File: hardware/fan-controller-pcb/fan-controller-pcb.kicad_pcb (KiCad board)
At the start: 2 copper layers, 100 x 130 mm, 53 parts, among them J1 Screw_Terminal_01x04, J2 nc3fdm3-v, J3 nc3mdm3-v, SW1 SW_SPDT, SW2 SW_DIP_x10, U1 MC7812BDTG, U2 MC7805CDTG, U3 MCP4922, U4 TLC272, U5 MAX485E

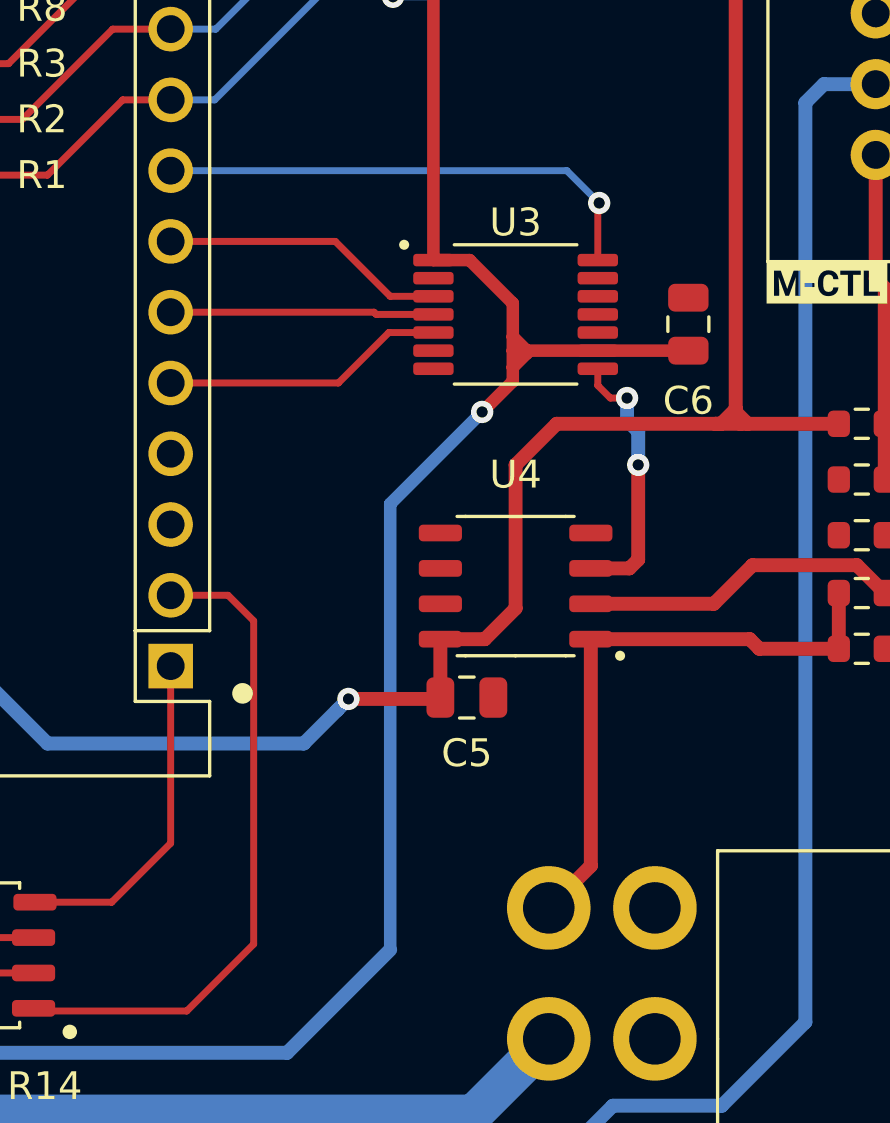
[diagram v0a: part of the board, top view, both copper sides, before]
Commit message: Fix the MCP4922 footprint and adapting the traces
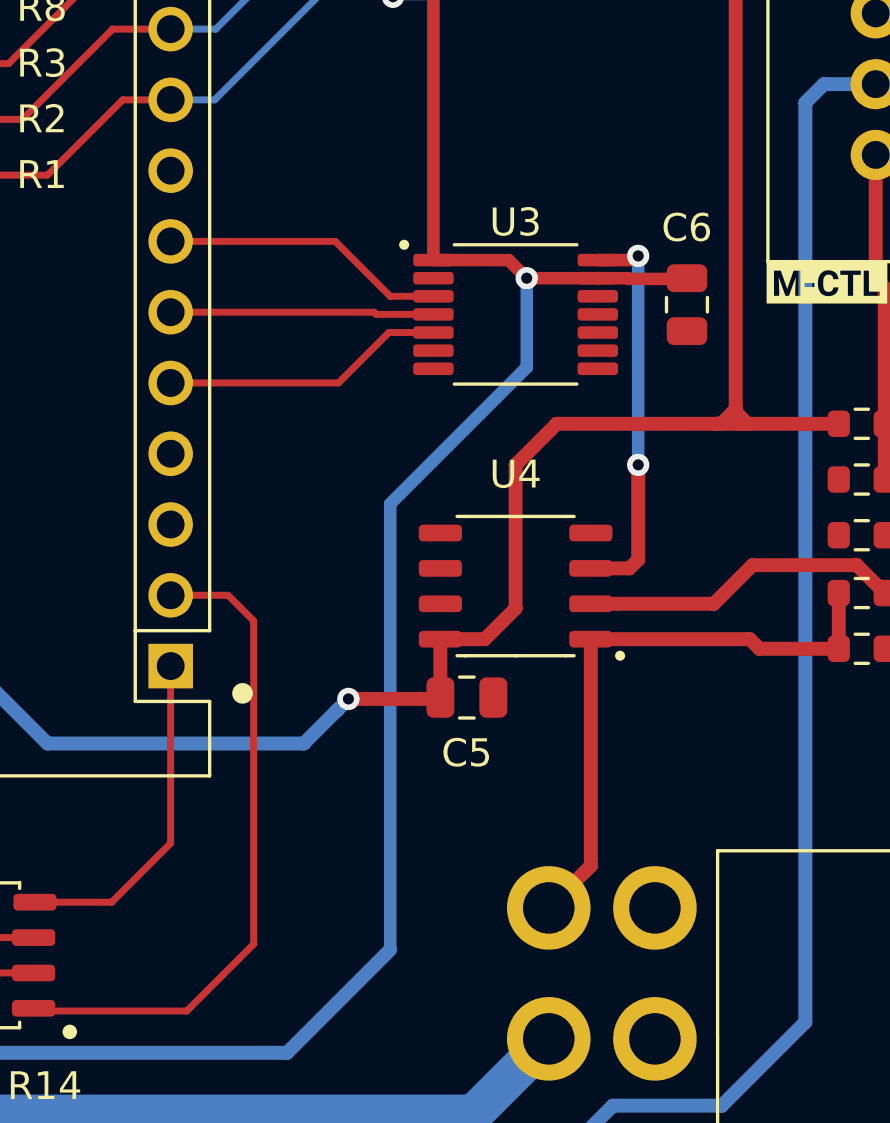
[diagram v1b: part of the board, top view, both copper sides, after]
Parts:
- moved C6 0.70 mm to (146.2, 92.7), turned to -90 degrees
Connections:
- A1 pad 8: Net-(A1-Pad8) -> unconnected-(A1-Pad8)
- R15 pad 1: Net-(R15-Pad1) -> 0-10V_Fan_Control
- R15 pad 2: 0-10V_Fan_Control -> Net-(R17-Pad1)
- R17 pad 1: 0-10V_Fan_Control -> Net-(R17-Pad1)
- U3 pad 8: Net-(A1-Pad8) -> unconnected-(U3-Pad8)
- U4 pad 2: Net-(R15-Pad1) -> Net-(R17-Pad1)
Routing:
- net Net-(A1-Pad8): track 17.9 -> 0.00 mm, vias 1 -> 0
- net Net-(R17-Pad1): track 0.00 -> 11.5 mm
- net Net-(R15-Pad1): track 11.5 -> 0.00 mm
- net Net-(U3-Pad14): track 9.63 -> 14.2 mm
- net +5V: track 140.1 -> 139.3 mm

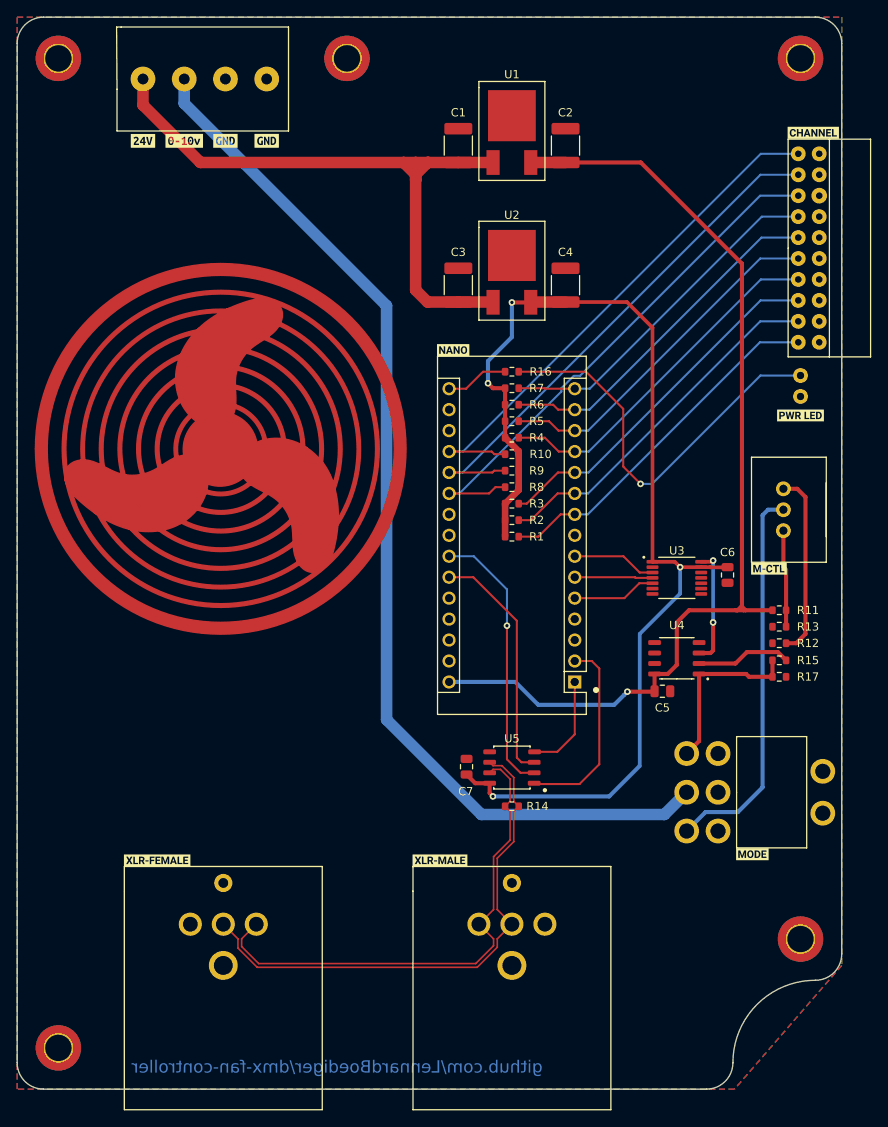
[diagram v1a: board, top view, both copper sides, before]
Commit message: minor routing improvements and adding gerber files
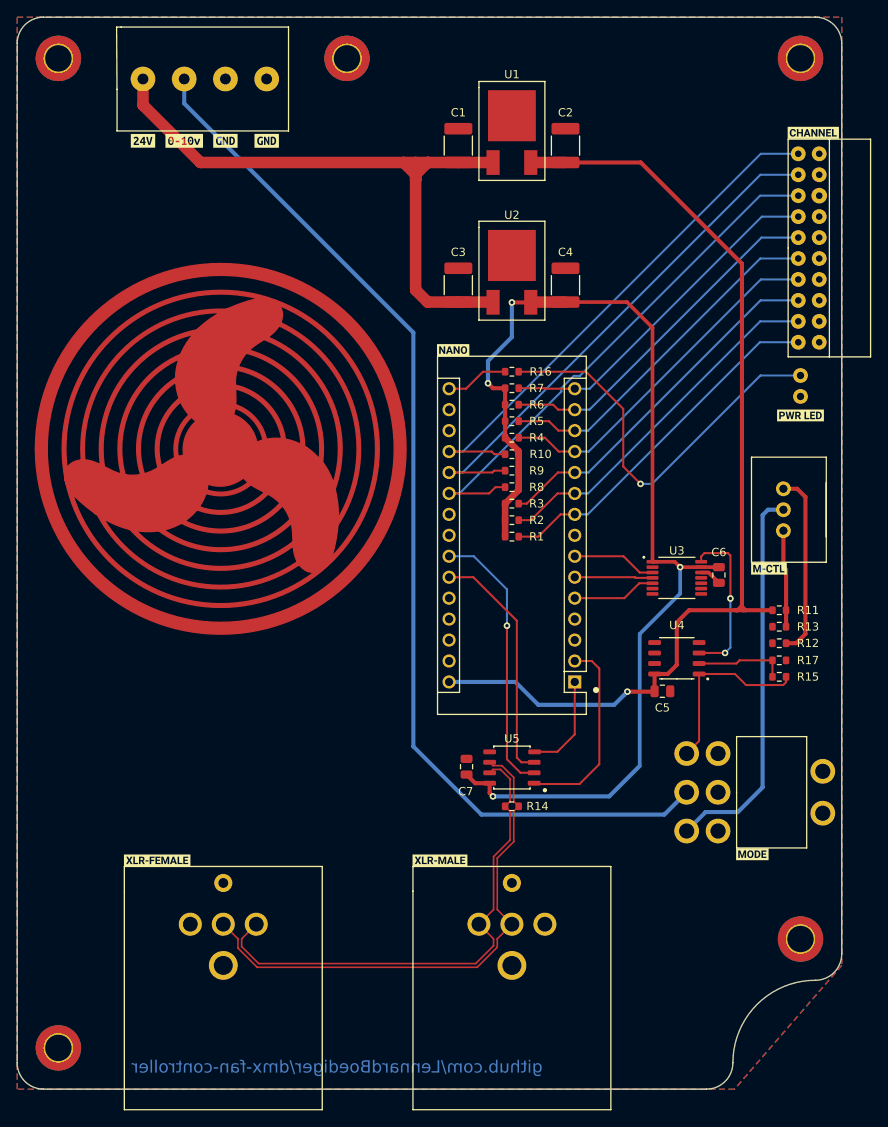
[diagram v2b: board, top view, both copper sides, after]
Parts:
- moved R15 2.00 mm to (152.4, 105.0)
- moved R17 2.00 mm to (152.4, 103.0)
- moved C6 1.05 mm to (145.1, 92.7)
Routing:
- net Net-(U3-Pad14): track 14.2 -> 19.7 mm
- net GND: track 0.00 -> 2.67 mm
- net +5V: track 139.3 -> 138.2 mm
- net 0-10V_Fan_Control: track 21.3 -> 22.2 mm

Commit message: update HW-Rev to  v2
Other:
- board text added: "DMX FAN CONTROLLER Rev: v2"
- board text removed: "DMX FAN CONTROLLER Rev: v1"
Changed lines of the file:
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@@
     (effects (font (size 1 1) (thickness 0.15)) (justify left mirror))
   )
-  (gr_text "DMX FAN CONTROLLER Rev: v1" (at 147.2 30) (layer "B.SilkS")
+  (gr_text "DMX FAN CONTROLLER Rev: v2" (at 147.2 30) (layer "B.SilkS")
     (effects (font (size 1.5 1.5) (thickness 0.3)) (justify left mirror))
   )
